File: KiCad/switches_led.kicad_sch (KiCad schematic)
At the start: 48 parts, among them Q2 2N3904, Q3 2N3904, Q4 2N3904, Q5 2N3904, Q6 2N3904, Q7 2N3904, Q8 2N3904, Q9 2N3904, SW1 SW_Nidec_CAS-120A1, SW2 SW_Nidec_CAS-120A1, SW3 SW_Nidec_CAS-120A1, SW4 SW_Nidec_CAS-120A1, SW5 SW_Nidec_CAS-120A1, SW6 SW_Nidec_CAS-120A1, SW7 SW_Nidec_CAS-120A1, SW8 SW_Nidec_CAS-120A1

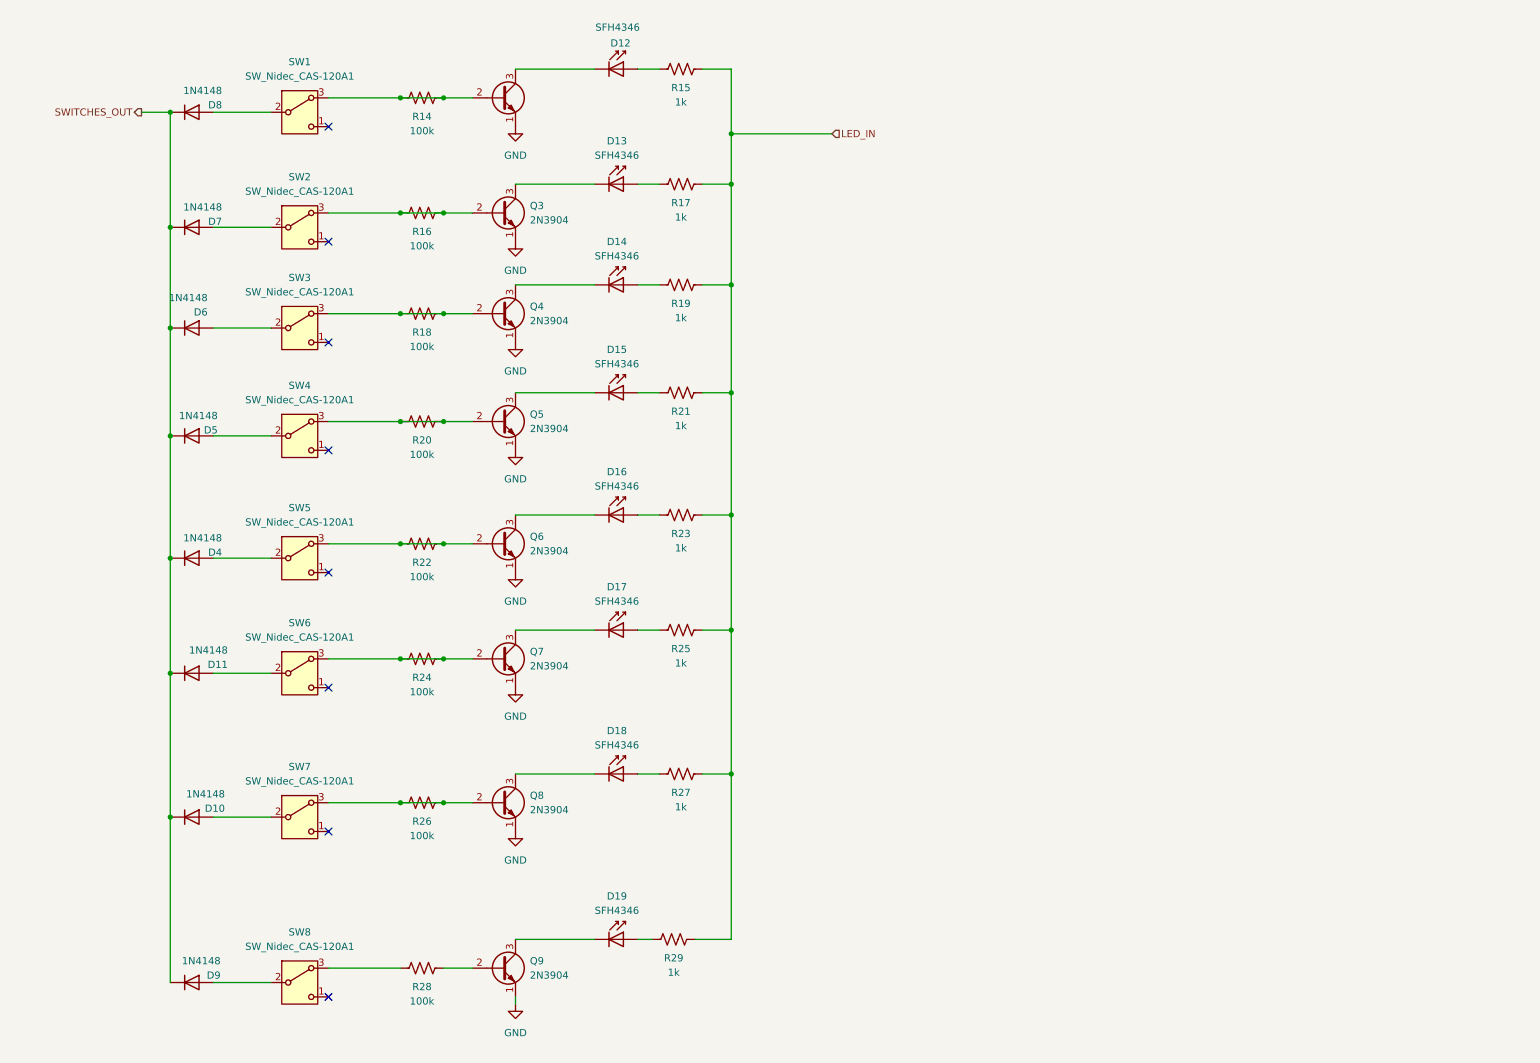
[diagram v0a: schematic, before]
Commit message: refactor(kicad): move switch/LED driver logic into switches_led sheet
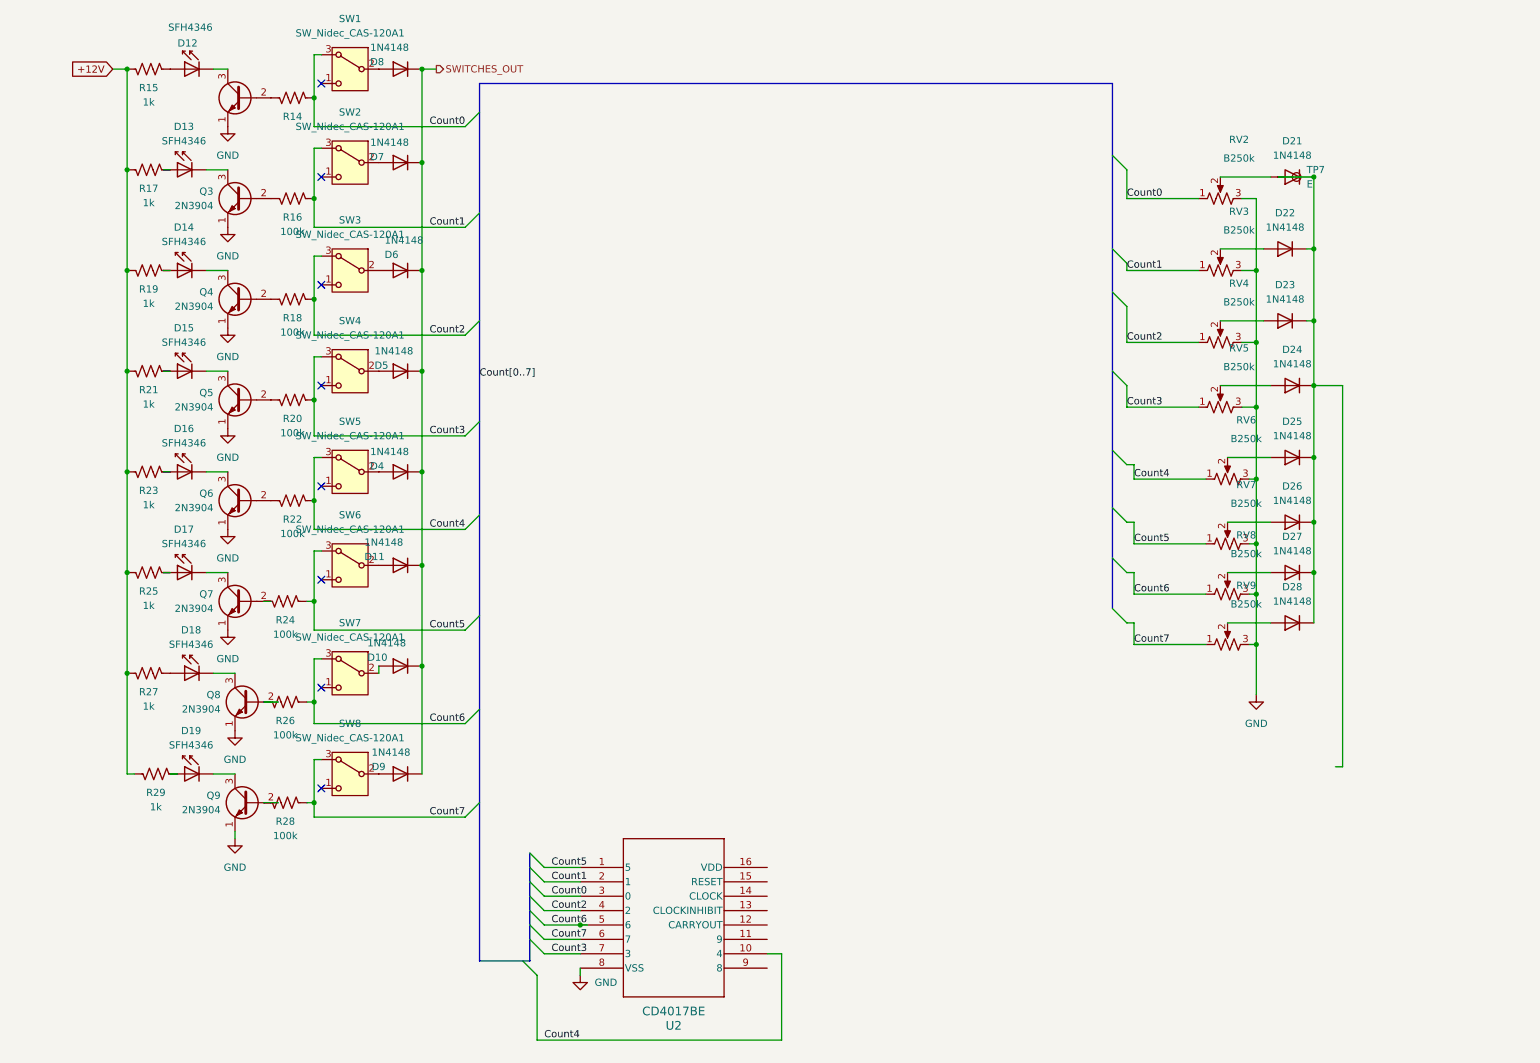
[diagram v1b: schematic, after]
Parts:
- added D21, D22, D23, D24, D25, D26, D27, D28: 1N4148, Diode_THT:D_DO-35_SOD27_P7.62mm_Horizontal, symbol Diode:1N4148
- added RV2, RV3, RV4, RV5, RV6, RV7, RV8, RV9: B250k, symbol Device:R_Potentiometer_US
- added TP7: E, symbol Connector:TestPoint
- added U2: CD4017BE, N16, symbol Eurorack:CD4017BE
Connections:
- net GND: now also RV2.3, RV3.3, RV4.3, RV5.3, RV6.3, RV7.3, RV8.3, RV9.3, U2.8 (VSS)
- net at Q2.2 (B), R14.1: no longer R14.2, SW1.3 (A)
- net at Q7.2 (B), R24.1: no longer R24.2, SW6.3 (A)
- net at Q8.2 (B), R26.1: no longer R26.2, SW7.3 (A)
- net Count7: now reaches R28.2, SW8.3 (A)
- net Count7: now also RV9.1, U2.6 (7)
- net at Q5.2 (B), R20.1: no longer R20.2, SW4.3 (A)
- net at Q3.2 (B), R16.1: no longer R16.2, SW2.3 (A)
- net at Q4.2 (B), R18.1: no longer R18.2, SW3.3 (A)
- net at Q6.2 (B), R22.1: no longer R22.2, SW5.3 (A)
- net LED_IN renamed +12V
- new net: D26.2 (A), RV7.2
- new net: D21.2 (A), RV2.2
- new net: D21.1 (K), D22.1 (K), D23.1 (K), D24.1 (K), D25.1 (K), D26.1 (K), D27.1 (K), D28.1 (K), TP7.1
- new net: D28.2 (A), RV9.2
- new net: D27.2 (A), RV8.2
- new net: D25.2 (A), RV6.2
- new net: D22.2 (A), RV3.2
- new net: D23.2 (A), RV4.2
- new net: D24.2 (A), RV5.2
- new net Count0: R14.2, RV2.1, SW1.3 (A), U2.3 (0)
- new net Count1: R16.2, RV3.1, SW2.3 (A), U2.2 (1)
- new net Count2: R18.2, RV4.1, SW3.3 (A), U2.4 (2)
- new net Count3: R20.2, RV5.1, SW4.3 (A), U2.7 (3)
- new net Count4: R22.2, RV6.1, SW5.3 (A), U2.10 (4)
- new net Count5: R24.2, RV7.1, SW6.3 (A), U2.1 (5)
- new net Count6: R26.2, RV8.1, SW7.3 (A), U2.5 (6)
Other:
- moved on the sheet: D10, D11, D12, D13, D14, D15, D16, D17, D18, D19, D4, D5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

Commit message: refactor(kicad): finishing root
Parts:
- removed TP7: E, symbol Connector:TestPoint
- added C9: 100nF, Capacitor_SMD:C_0805_2012Metric_Pad1.18x1.45mm_HandSolder, symbol Device:C
- added D29: 1N4148, Diode_THT:D_DO-35_SOD27_P7.62mm_Horizontal, symbol Diode:1N4148
- added R31: 100k, symbol Device:R_US
- added SW9: SW_Rotary_1x9_MP, symbol Switch:SW_Rotary_1x9_MP
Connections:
- net +12V: now also U2.16 (VDD), C9.1
- net Count0: now also SW9.1
- net Count1: now also SW9.2
- net Count2: now also SW9.3
- net Count3: now also SW9.4
- net Count4: now also SW9.5
- net Count5: now also SW9.6
- net Count6: now also SW9.7
- net Count7: now also SW9.8
- net GND: now also U2.13 (CLOCKINHIBIT), C9.2, R31.1
- net CV OUT: now reaches D21.1 (K), D22.1 (K), D23.1 (K), D24.1 (K), D25.1 (K), D26.1 (K), D27.1 (K), D28.1 (K)
- net EXTERNAL CLOCK: now reaches U2.14 (CLOCK)
- net EXTERNAL RESET: now reaches U2.15 (RESET)
- net EXTERNAL RESET: now also D29.1 (K), R31.2
- net SWITCHES_OUT renamed GATE OUT
- new net: D29.2 (A), SW9.10
- no-connect marks 8 -> 13
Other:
- moved on the sheet: D10, D11, D12, D13, D14, D15, D16, D17, D18, D19, D22, D23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

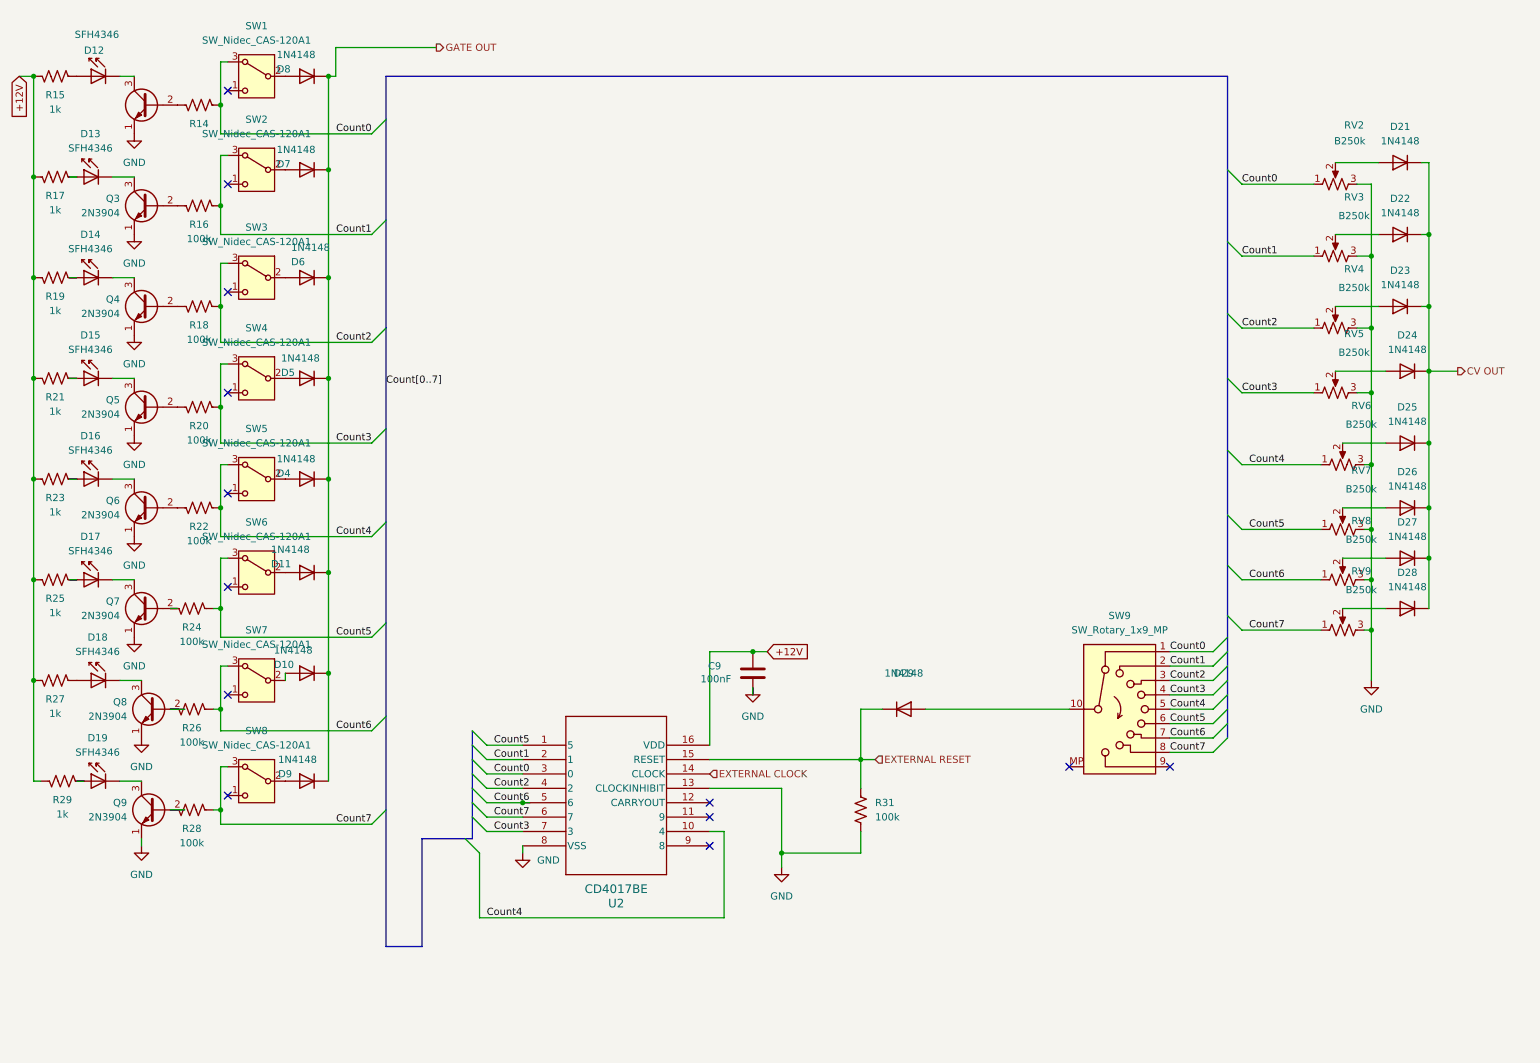
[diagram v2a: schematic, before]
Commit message: refactor(kicad): first ERC run
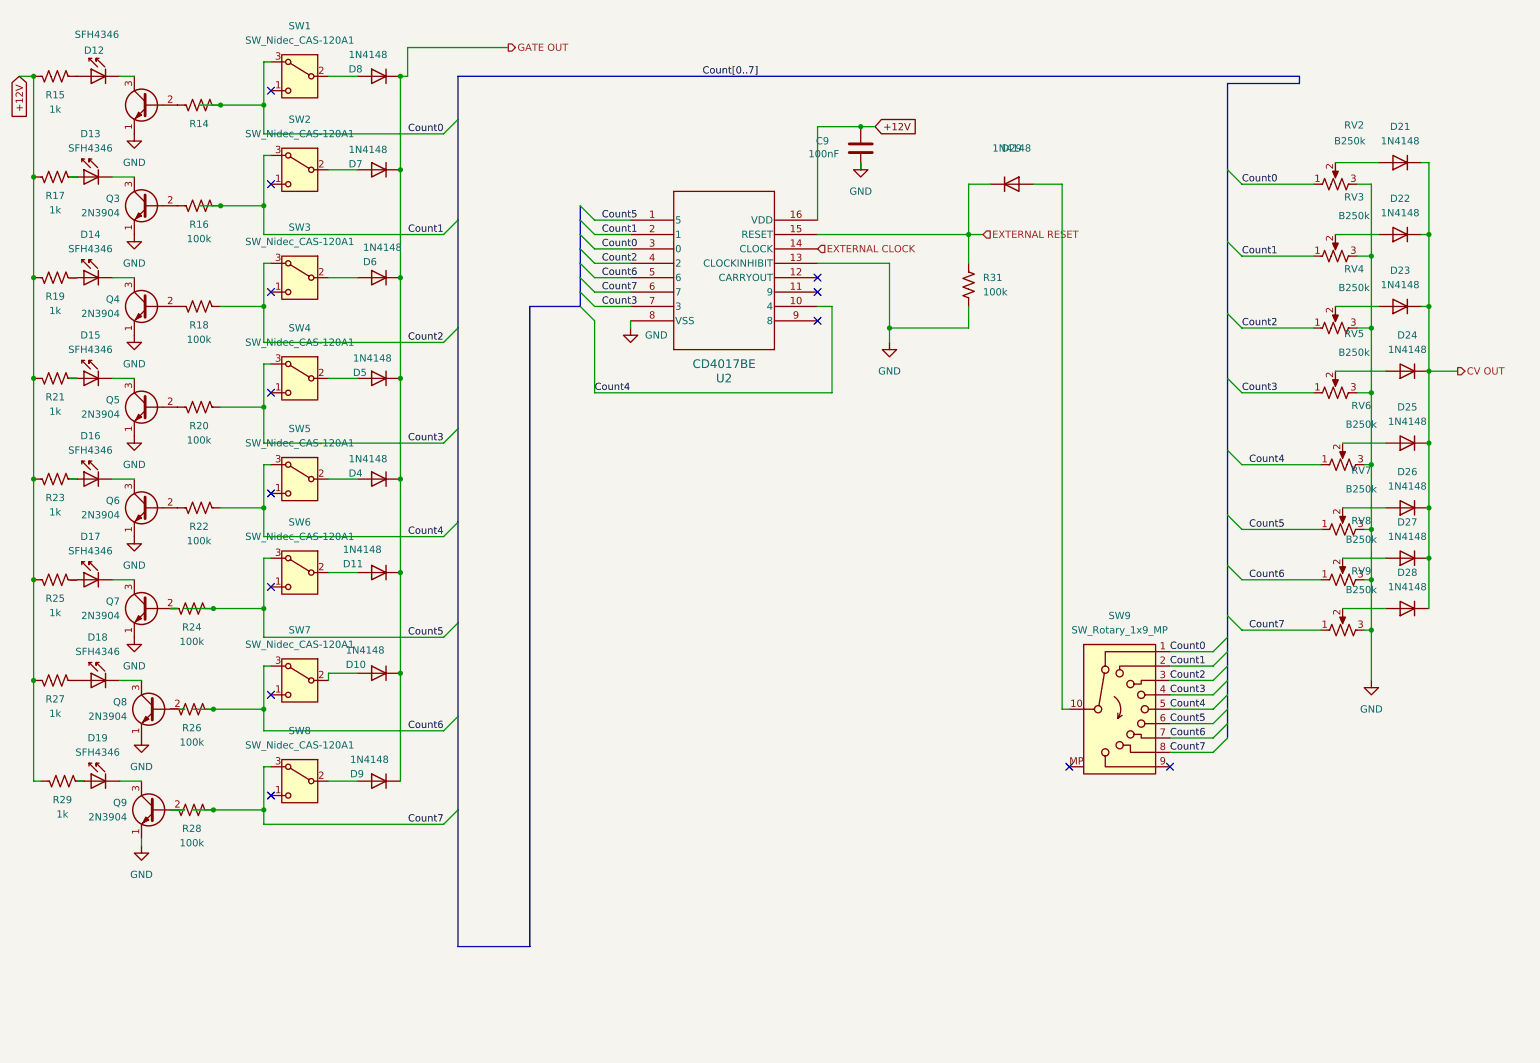
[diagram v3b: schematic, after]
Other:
- moved on the sheet: C9, D10, D11, D29, D4, D5, D6, D7, D8, D9, R31, SW1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

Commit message: Refine KiCad schematics for power, test points, and control values
  - replace schematic +12V/-12V global labels with proper power symbols
  - add GND test points and reorganize the power/IDC and main sequencer
  sheets
  - retune sequencer values including R33/R34 to 51k, R35 to 68k, C8 to
  1nF, and trim pots to 2k/5k
  - update switch/LED sheet labels and pot values, renaming LEDs by step
  and changing B250k controls to B100k
  - relax the KiCad four-way junction ERC setting in the project file
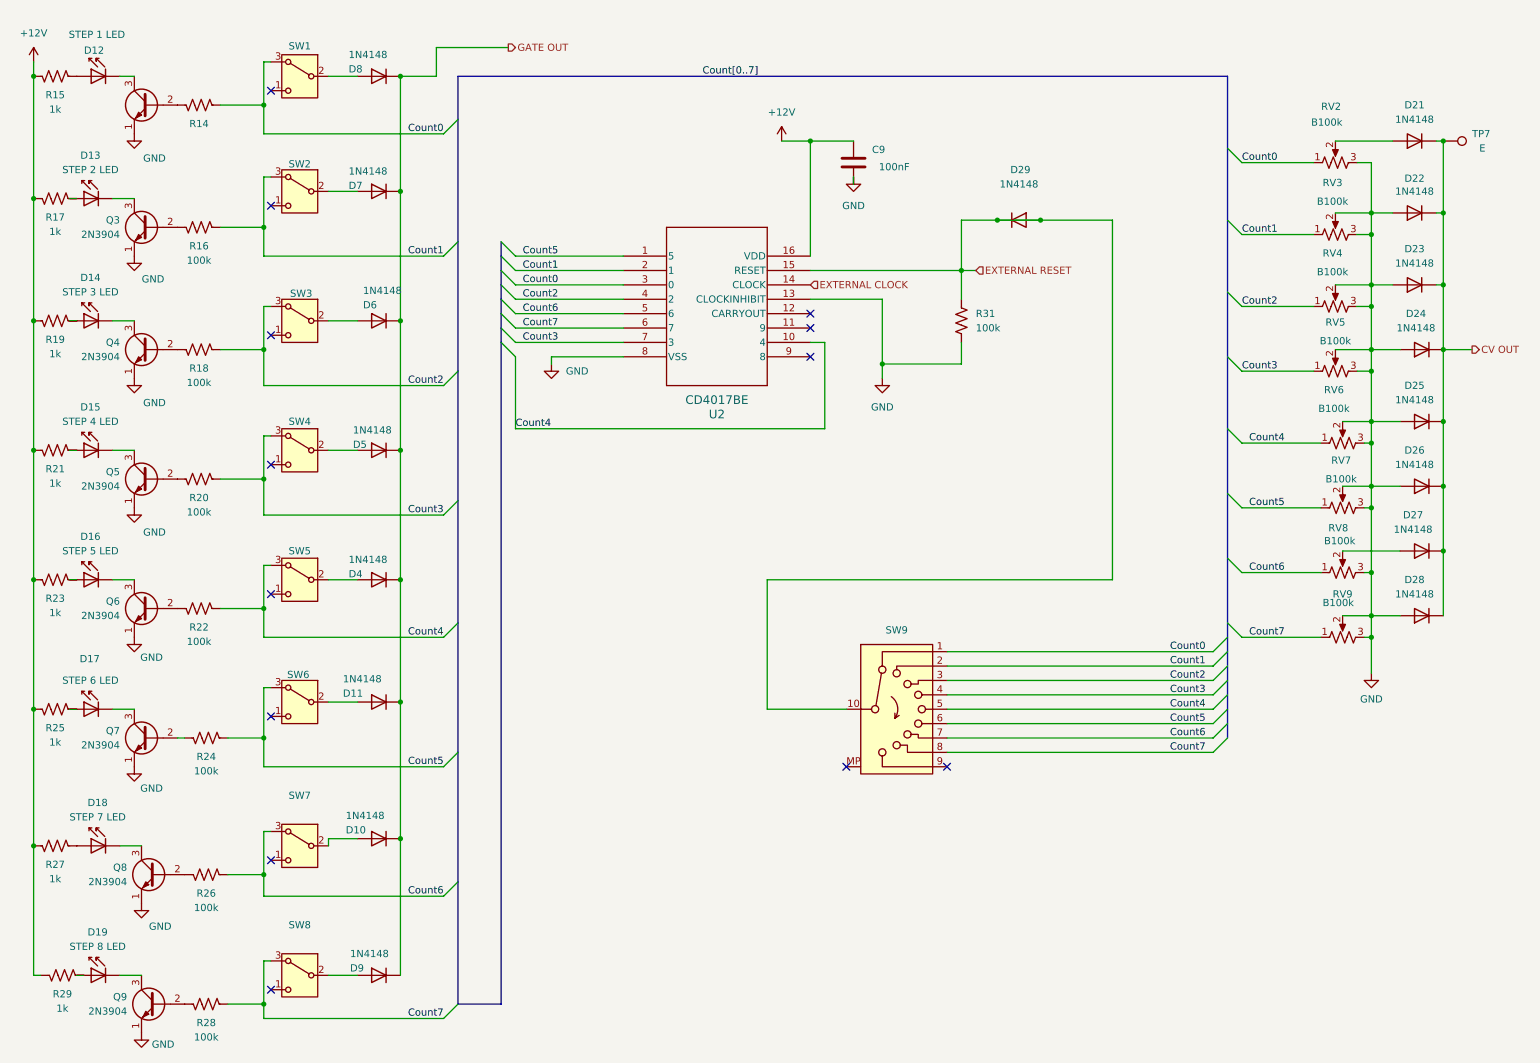
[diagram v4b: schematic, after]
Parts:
- added TP7: E, symbol Connector:TestPoint
- D12: value SFH4346 -> STEP 1 LED
- D13: value SFH4346 -> STEP 2 LED
- D14: value SFH4346 -> STEP 3 LED
- D15: value SFH4346 -> STEP 4 LED
- D16: value SFH4346 -> STEP 5 LED
- D17: value SFH4346 -> STEP 6 LED
- D18: value SFH4346 -> STEP 7 LED
- D19: value SFH4346 -> STEP 8 LED
- RV2, RV3, RV4, RV5, RV6, RV7, RV8, RV9: value B250k -> B100k
- SW1, SW2, SW3, SW4, SW5, SW6, SW7, SW8: value SW_Nidec_CAS-120A1 -> ~
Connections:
- net CV OUT: now also TP7.1
- net EXTERNAL RESET: now also D29.2 (A), SW9.10
- net GND: now also D22.2 (A), D23.2 (A), D24.2 (A), D25.2 (A), D26.2 (A), D28.2 (A), RV3.2, RV4.2, RV5.2, RV6.2, RV7.2, RV9.2
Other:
- moved on the sheet: C9, D10, D11, D13, D14, D15, D16, D17, D18, D19, D21, D22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
